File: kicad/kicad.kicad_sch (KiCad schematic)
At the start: 256 parts, among them J1 USB_B_Micro, J2 SWD, J3 pwr_led+, J4 pwr_led-, J5 caps_led+, J6 caps_led-, U1 AMS1117-3.3, Y1 16MGz, sw1 Esc, sw10 Z, sw100 N5, sw101 N6, sw102 N2, sw103 N1, sw104 N0, sw105 MPlay, sw106 MFwd, sw107 NSlash, sw108 NStar, sw109 N8, sw11 LCtrl, sw110 N9, sw111 NMinus, sw112 NPlus, sw113 NEnter, sw114 N3, sw115 NPeriod, sw12 LSys, sw13 F2, sw14 F3, sw15 2, sw16 3, sw17 W, sw18 E, sw19 S, sw2 F1, sw20 D, sw21 X, sw22 C, sw23 LAlt, sw24 THome, sw25 F4, sw26 F5, sw27 4, sw28 5, sw29 R, sw3 Tilda, sw30 T, sw31 F, sw32 G, sw33 V, sw34 B, sw35 LSpace, sw36 TLeft, sw37 F6, sw38 F7, sw39 6, sw4 1, sw40 7, sw41 Y, sw42 U, sw43 H, sw44 J, sw45 N, sw46 M, sw47 TUp, sw48 TDown, sw49 F8, sw5 Tab, sw50 F9, sw51 8, sw52 9, sw53 I, sw54 O, sw55 K, sw56 L, sw57 Comma, sw58 Period, sw59 RSpace, sw6 Q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

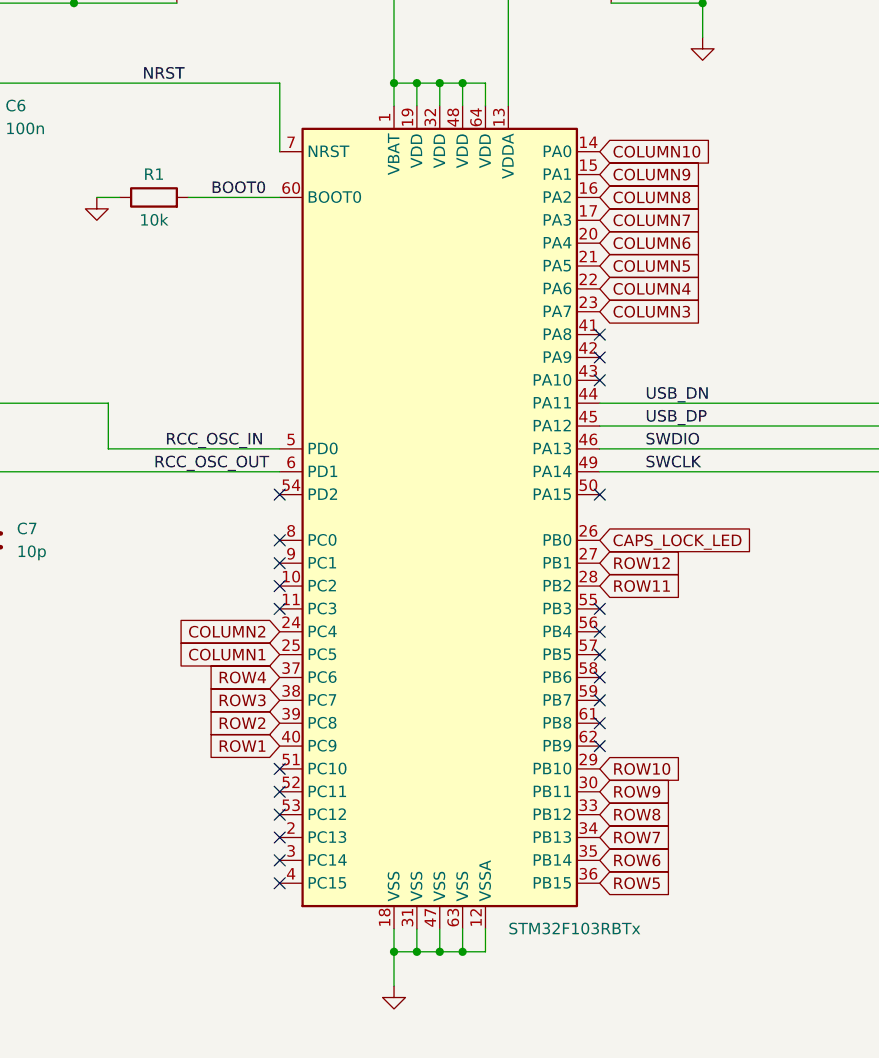
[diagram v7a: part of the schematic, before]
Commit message: Get rid of need for key signals on left side of board
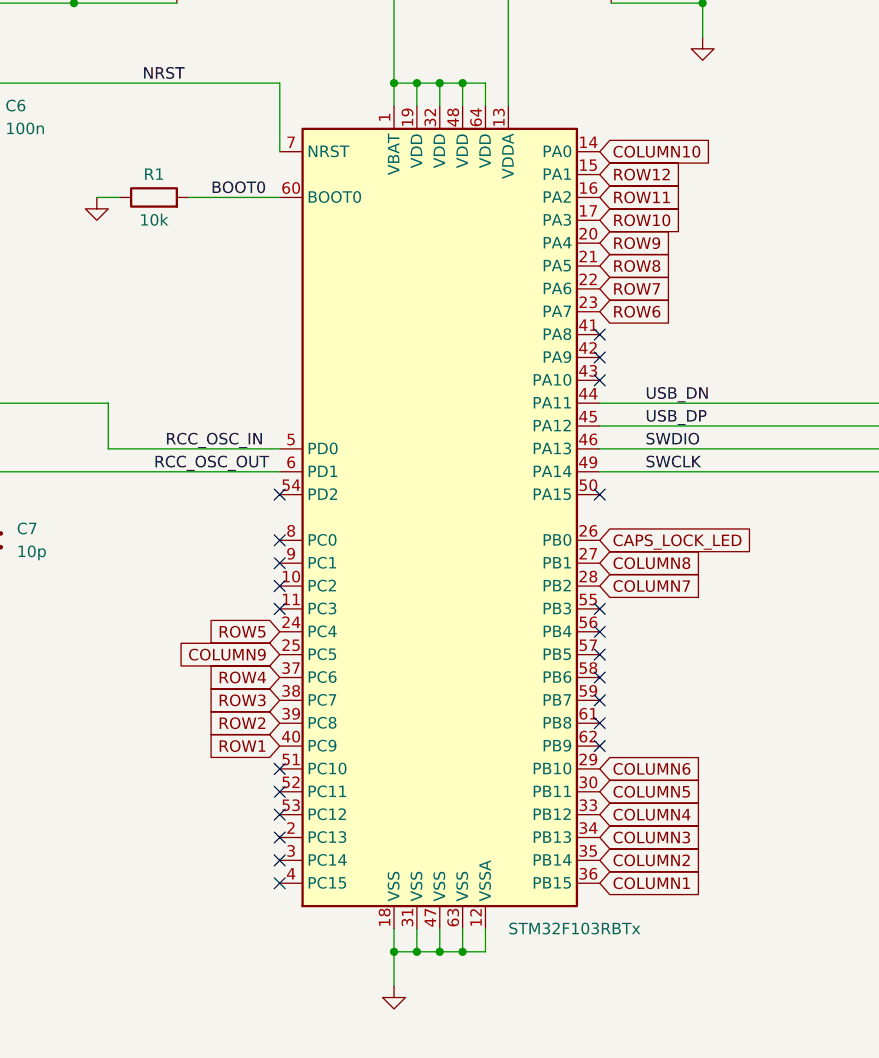
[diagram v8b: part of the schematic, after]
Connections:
- net COLUMN1: now also MCU1.36 (PB15); no longer MCU1.25 (PC5)
- net COLUMN2: now also MCU1.35 (PB14); no longer MCU1.24 (PC4)
- net COLUMN3: now also MCU1.34 (PB13); no longer MCU1.23 (PA7)
- net COLUMN4: now also MCU1.33 (PB12); no longer MCU1.22 (PA6)
- net COLUMN5: now also MCU1.30 (PB11); no longer MCU1.21 (PA5)
- net COLUMN6: now also MCU1.29 (PB10); no longer MCU1.20 (PA4)
- net COLUMN7: now also MCU1.28 (PB2); no longer MCU1.17 (PA3)
- net COLUMN8: now also MCU1.27 (PB1); no longer MCU1.16 (PA2)
- net COLUMN9: now also MCU1.25 (PC5); no longer MCU1.15 (PA1)
- net ROW10: now also MCU1.17 (PA3); no longer MCU1.29 (PB10)
- net ROW11: now also MCU1.16 (PA2); no longer MCU1.28 (PB2)
- net ROW12: now also MCU1.15 (PA1); no longer MCU1.27 (PB1)
- net ROW5: now also MCU1.24 (PC4); no longer MCU1.36 (PB15)
- net ROW6: now also MCU1.23 (PA7); no longer MCU1.35 (PB14)
- net ROW7: now also MCU1.22 (PA6); no longer MCU1.34 (PB13)
- net ROW8: now also MCU1.21 (PA5); no longer MCU1.33 (PB12)
- net ROW9: now also MCU1.20 (PA4); no longer MCU1.30 (PB11)
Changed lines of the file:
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@@
     )
   )
-  (global_label "COLUMN7" (shape input) (at 381 82.55 0) (fields_autoplaced)
-    (effects (font (size 1.27 1.27)) (justify left))
-    (property "Intersheet References" "${INTERSHEET_REFS}" (id 0) (at 392.3636 82.4706 0)
+  (global_label "COLUMN7" (shape input) (at 381 123.19 0) (fields_autoplaced)
+    (effects (font (size 1.27 1.27)) (justify left))
+    (property "Intersheet References" "${INTERSHEET_REFS}" (id 0) (at 392.3636 123.1106 0)
       (effects (font (size 1.27 1.27)) (justify left) hide)
     )
@@
     )
   )
-  (global_label "ROW10" (shape input) (at 381 143.51 0) (fields_autoplaced)
-    (effects (font (size 1.27 1.27)) (justify left))
-    (property "Intersheet References" "${INTERSHEET_REFS}" (id 0) (at 389.8841 143.4306 0)
-      (effects (font (size 1.27 1.27)) (justify left) hide)
-    )
-  )
-  (global_label "COLUMN4" (shape input) (at 381 90.17 0) (fields_autoplaced)
-    (effects (font (size 1.27 1.27)) (justify left))
-    (property "Intersheet References" "${INTERSHEET_REFS}" (id 0) (at 392.3636 90.0906 0)
-      (effects (font (size 1.27 1.27)) (justify left) hide)
-    )
-  )
-  (global_label "ROW7" (shape input) (at 381 151.13 0) (fields_autoplaced)
-    (effects (font (size 1.27 1.27)) (justify left))
-    (property "Intersheet References" "${INTERSHEET_REFS}" (id 0) (at 388.6745 151.0506 0)
+  (global_label "ROW10" (shape input) (at 381 82.55 0) (fields_autoplaced)
+    (effects (font (size 1.27 1.27)) (justify left))
+    (property "Intersheet References" "${INTERSHEET_REFS}" (id 0) (at 389.8841 82.4706 0)
+      (effects (font (size 1.27 1.27)) (justify left) hide)
+    )
+  )
+  (global_label "COLUMN4" (shape input) (at 381 148.59 0) (fields_autoplaced)
+    (effects (font (size 1.27 1.27)) (justify left))
+    (property "Intersheet References" "${INTERSHEET_REFS}" (id 0) (at 392.3636 148.5106 0)
+      (effects (font (size 1.27 1.27)) (justify left) hide)
+    )
+  )
+  (global_label "ROW7" (shape input) (at 381 90.17 0) (fields_autoplaced)
+    (effects (font (size 1.27 1.27)) (justify left))
+    (property "Intersheet References" "${INTERSHEET_REFS}" (id 0) (at 388.6745 90.0906 0)
       (effects (font (size 1.27 1.27)) (justify left) hide)
     )
@@
     )
   )
-  (global_label "COLUMN9" (shape input) (at 381 77.47 0) (fields_autoplaced)
-    (effects (font (size 1.27 1.27)) (justify left))
-    (property "Intersheet References" "${INTERSHEET_REFS}" (id 0) (at 392.3636 77.3906 0)
-      (effects (font (size 1.27 1.27)) (justify left) hide)
-    )
-  )
-  (global_label "COLUMN8" (shape input) (at 381 80.01 0) (fields_autoplaced)
-    (effects (font (size 1.27 1.27)) (justify left))
-    (property "Intersheet References" "${INTERSHEET_REFS}" (id 0) (at 392.3636 79.9306 0)
-      (effects (font (size 1.27 1.27)) (justify left) hide)
-    )
-  )
-  (global_label "ROW9" (shape input) (at 381 146.05 0) (fields_autoplaced)
-    (effects (font (size 1.27 1.27)) (justify left))
-    (property "Intersheet References" "${INTERSHEET_REFS}" (id 0) (at 388.6745 145.9706 0)
+  (global_label "COLUMN9" (shape input) (at 345.44 130.81 180) (fields_autoplaced)
+    (effects (font (size 1.27 1.27)) (justify right))
+    (property "Intersheet References" "${INTERSHEET_REFS}" (id 0) (at 334.0764 130.8894 0)
+      (effects (font (size 1.27 1.27)) (justify right) hide)
+    )
+  )
+  (global_label "COLUMN8" (shape input) (at 381 120.65 0) (fields_autoplaced)
+    (effects (font (size 1.27 1.27)) (justify left))
+    (property "Intersheet References" "${INTERSHEET_REFS}" (id 0) (at 392.3636 120.5706 0)
+      (effects (font (size 1.27 1.27)) (justify left) hide)
+    )
+  )
+  (global_label "ROW9" (shape input) (at 381 85.09 0) (fields_autoplaced)
+    (effects (font (size 1.27 1.27)) (justify left))
+    (property "Intersheet References" "${INTERSHEET_REFS}" (id 0) (at 388.6745 85.0106 0)
       (effects (font (size 1.27 1.27)) (justify left) hide)
     )
@@
     )
   )
-  (global_label "COLUMN3" (shape input) (at 381 92.71 0) (fields_autoplaced)
-    (effects (font (size 1.27 1.27)) (justify left))
-    (property "Intersheet References" "${INTERSHEET_REFS}" (id 0) (at 392.3636 92.6306 0)
+  (global_label "COLUMN3" (shape input) (at 381 151.13 0) (fields_autoplaced)
+    (effects (font (size 1.27 1.27)) (justify left))
+    (property "Intersheet References" "${INTERSHEET_REFS}" (id 0) (at 392.3636 151.0506 0)
       (effects (font (size 1.27 1.27)) (justify left) hide)
     )
@@
     )
   )
-  (global_label "ROW8" (shape input) (at 381 148.59 0) (fields_autoplaced)
-    (effects (font (size 1.27 1.27)) (justify left))
-    (property "Intersheet References" "${INTERSHEET_REFS}" (id 0) (at 388.6745 148.5106 0)
-      (effects (font (size 1.27 1.27)) (justify left) hide)
-    )
-  )
-  (global_label "COLUMN2" (shape input) (at 345.44 128.27 180) (fields_autoplaced)
-    (effects (font (size 1.27 1.27)) (justify right))
-    (property "Intersheet References" "${INTERSHEET_REFS}" (id 0) (at 334.0764 128.1906 0)
-      (effects (font (size 1.27 1.27)) (justify right) hide)
-    )
-  )
-  (global_label "ROW12" (shape input) (at 381 120.65 0) (fields_autoplaced)
-    (effects (font (size 1.27 1.27)) (justify left))
-    (property "Intersheet References" "${INTERSHEET_REFS}" (id 0) (at 389.8841 120.5706 0)
+  (global_label "ROW8" (shape input) (at 381 87.63 0) (fields_autoplaced)
+    (effects (font (size 1.27 1.27)) (justify left))
+    (property "Intersheet References" "${INTERSHEET_REFS}" (id 0) (at 388.6745 87.5506 0)
+      (effects (font (size 1.27 1.27)) (justify left) hide)
+    )
+  )
+  (global_label "COLUMN2" (shape input) (at 381 153.67 0) (fields_autoplaced)
+    (effects (font (size 1.27 1.27)) (justify left))
+    (property "Intersheet References" "${INTERSHEET_REFS}" (id 0) (at 392.3636 153.7494 0)
+      (effects (font (size 1.27 1.27)) (justify left) hide)
+    )
+  )
+  (global_label "ROW12" (shape input) (at 381 77.47 0) (fields_autoplaced)
+    (effects (font (size 1.27 1.27)) (justify left))
+    (property "Intersheet References" "${INTERSHEET_REFS}" (id 0) (at 389.8841 77.3906 0)
       (effects (font (size 1.27 1.27)) (justify left) hide)
     )
@@
     )
   )
-  (global_label "ROW6" (shape input) (at 381 153.67 0) (fields_autoplaced)
-    (effects (font (size 1.27 1.27)) (justify left))
-    (property "Intersheet References" "${INTERSHEET_REFS}" (id 0) (at 388.6745 153.5906 0)
-      (effects (font (size 1.27 1.27)) (justify left) hide)
-    )
-  )
-  (global_label "COLUMN1" (shape input) (at 345.44 130.81 180) (fields_autoplaced)
-    (effects (font (size 1.27 1.27)) (justify right))
-    (property "Intersheet References" "${INTERSHEET_REFS}" (id 0) (at 334.0764 130.7306 0)
-      (effects (font (size 1.27 1.27)) (justify right) hide)
+  (global_label "ROW6" (shape input) (at 381 92.71 0) (fields_autoplaced)
+    (effects (font (size 1.27 1.27)) (justify left))
+    (property "Intersheet References" "${INTERSHEET_REFS}" (id 0) (at 388.6745 92.6306 0)
+      (effects (font (size 1.27 1.27)) (justify left) hide)
+    )
+  )
+  (global_label "COLUMN1" (shape input) (at 381 156.21 0) (fields_autoplaced)
+    (effects (font (size 1.27 1.27)) (justify left))
+    (property "Intersheet References" "${INTERSHEET_REFS}" (id 0) (at 392.3636 156.2894 0)
+      (effects (font (size 1.27 1.27)) (justify left) hide)
     )
   )
@@
     )
   )
-  (global_label "ROW5" (shape input) (at 381 156.21 0) (fields_autoplaced)
-    (effects (font (size 1.27 1.27)) (justify left))
-    (property "Intersheet References" "${INTERSHEET_REFS}" (id 0) (at 388.6745 156.1306 0)
-      (effects (font (size 1.27 1.27)) (justify left) hide)
-    )
-  )
-  (global_label "ROW11" (shape input) (at 381 123.19 0) (fields_autoplaced)
-    (effects (font (size 1.27 1.27)) (justify left))
-    (property "Intersheet References" "${INTERSHEET_REFS}" (id 0) (at 389.8841 123.1106 0)
+  (global_label "ROW5" (shape input) (at 345.44 128.27 180) (fields_autoplaced)
+    (effects (font (size 1.27 1.27)) (justify right))
+    (property "Intersheet References" "${INTERSHEET_REFS}" (id 0) (at 337.7655 128.3494 0)
+      (effects (font (size 1.27 1.27)) (justify right) hide)
+    )
+  )
+  (global_label "ROW11" (shape input) (at 381 80.01 0) (fields_autoplaced)
+    (effects (font (size 1.27 1.27)) (justify left))
+    (property "Intersheet References" "${INTERSHEET_REFS}" (id 0) (at 389.8841 79.9306 0)
       (effects (font (size 1.27 1.27)) (justify left) hide)
     )
@@
     )
   )
-  (global_label "COLUMN6" (shape input) (at 381 85.09 0) (fields_autoplaced)
-    (effects (font (size 1.27 1.27)) (justify left))
-    (property "Intersheet References" "${INTERSHEET_REFS}" (id 0) (at 392.3636 85.0106 0)
+  (global_label "COLUMN6" (shape input) (at 381 143.51 0) (fields_autoplaced)
+    (effects (font (size 1.27 1.27)) (justify left))
+    (property "Intersheet References" "${INTERSHEET_REFS}" (id 0) (at 392.3636 143.4306 0)
       (effects (font (size 1.27 1.27)) (justify left) hide)
     )
@@
     )
   )
-  (global_label "COLUMN5" (shape input) (at 381 87.63 0) (fields_autoplaced)
-    (effects (font (size 1.27 1.27)) (justify left))
-    (property "Intersheet References" "${INTERSHEET_REFS}" (id 0) (at 392.3636 87.5506 0)
-      (effects (font (size 1.27 1.27)) (justify left) hide)
-    )
+  (global_label "COLUMN5" (shape input) (at 381 146.05 0) (fields_autoplaced)
+    (effects (font (size 1.27 1.27)) (justify left))
+    (property "Intersheet References" "${INTERSHEET_REFS}" (id 0) (at 392.3636 145.9706 0)
+      (effects (font (size 1.27 1.27)) (justify left) hide)
+    )
